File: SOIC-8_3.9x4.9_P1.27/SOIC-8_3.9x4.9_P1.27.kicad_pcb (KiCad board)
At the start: 2 copper layers, 17.8 x 10.2 mm, 6 parts, among them J101 Conn_01x26, J102 Conn_01x26, J103 Conn_01x26, J104 Conn_01x26, U101 SOIC-8

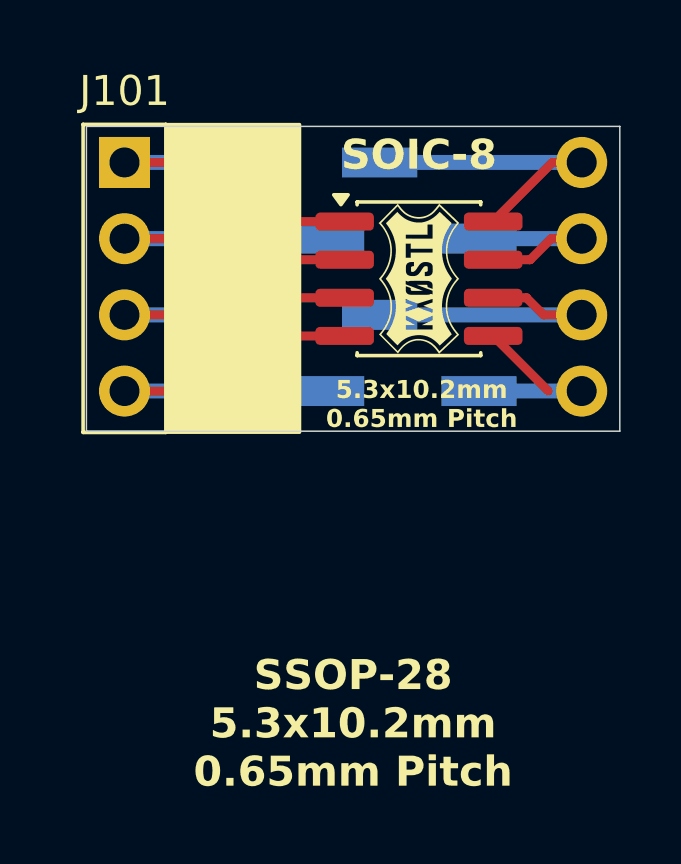
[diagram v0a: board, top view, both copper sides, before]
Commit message: Fixed SOIC-8 labels
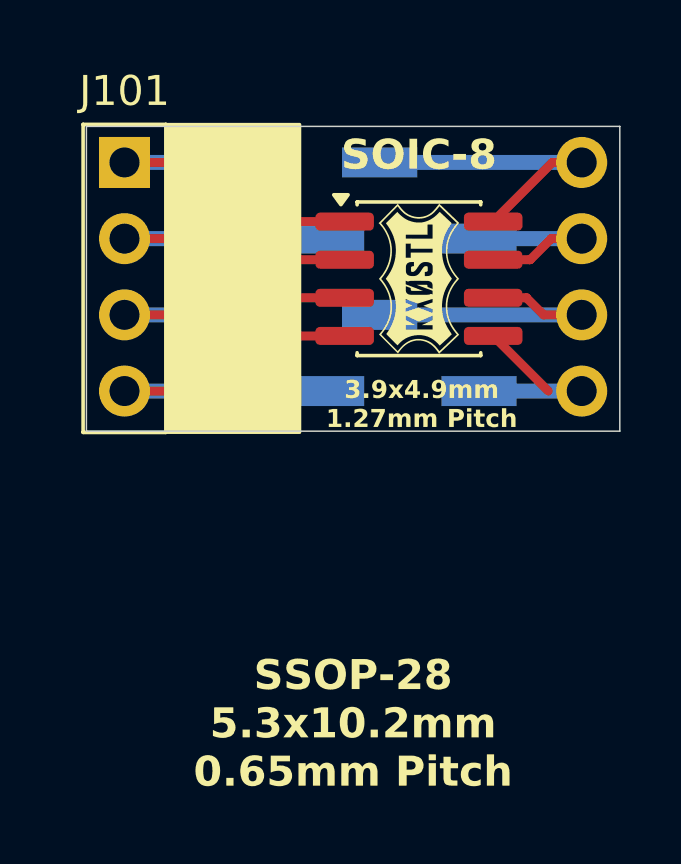
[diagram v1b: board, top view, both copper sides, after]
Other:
- board text added: "3.9x4.9mm 1.27mm Pitch"
- board text removed: "5.3x10.2mm 0.65mm Pitch"
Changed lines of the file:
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@@
 		)
 	)
-	(gr_text "5.3x10.2mm\n0.65mm Pitch"
+	(gr_text "3.9x4.9mm\n1.27mm Pitch"
 		(at 129.032 103.886 0)
 		(layer "F.SilkS")
